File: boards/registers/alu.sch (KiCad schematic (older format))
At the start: 1 part, among them J1 ALU

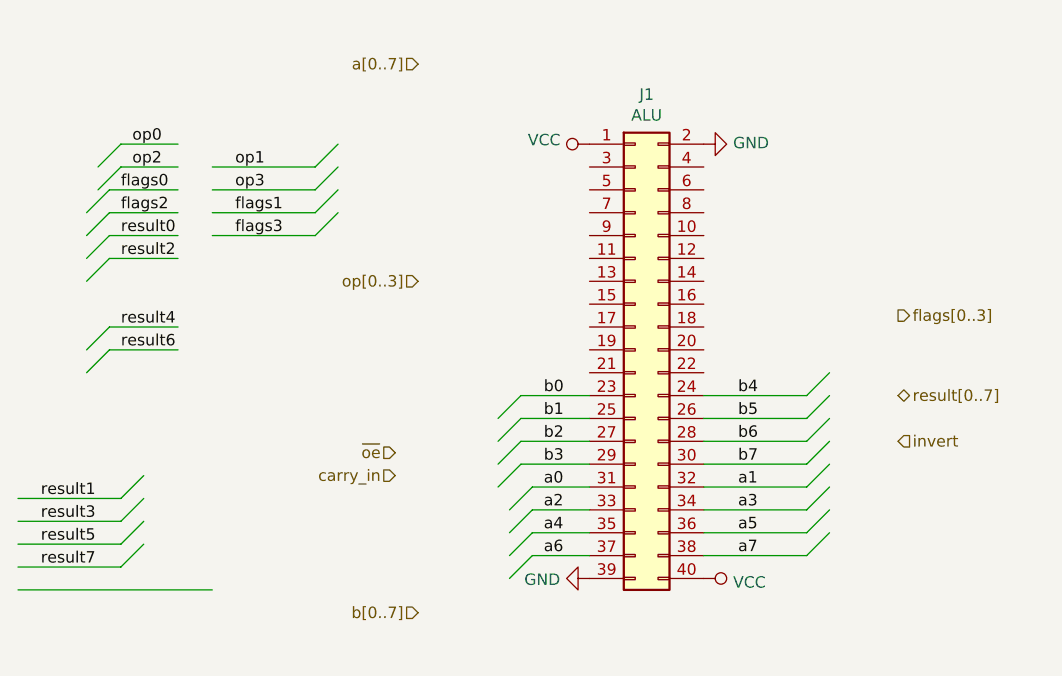
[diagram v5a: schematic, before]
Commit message: CPU registers board
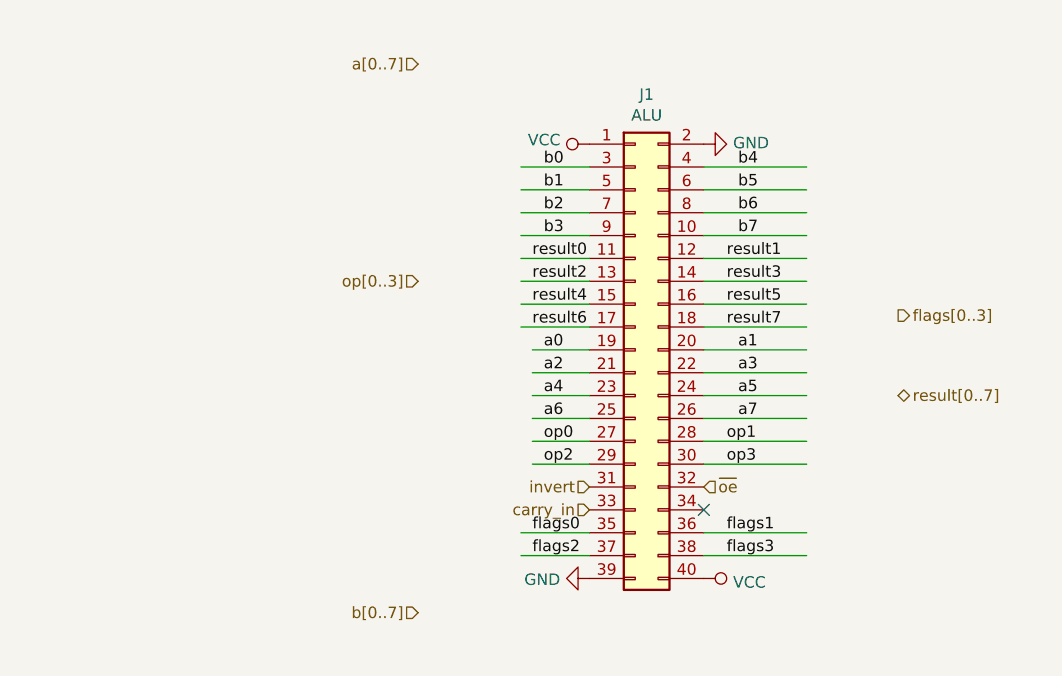
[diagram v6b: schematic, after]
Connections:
- wire segments 33 -> 32
- no-connect marks 0 -> 1
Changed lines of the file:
@@
 Text HLabel 3250 2400 0    50   Input ~ 0
 op[0..3]
-Text HLabel 3150 3150 0    50   Input ~ 0
+Text HLabel 4500 3300 2    50   Input ~ 0
 ~oe
-Text HLabel 3150 3250 0    50   Input ~ 0
+Text HLabel 4000 3400 0    50   Input ~ 0
 carry_in
-Text HLabel 5350 3100 2    50   Input ~ 0
+Text HLabel 4000 3300 0    50   Input ~ 0
 invert
 Text HLabel 5350 2900 2    50   3State ~ 0
@@
 	0    1    1    0
 $EndComp
-Entry Wire Line
-	3650 3400 3750 3300
-Entry Wire Line
-	3650 3500 3750 3400
-Entry Wire Line
-	3650 3600 3750 3500
-Entry Wire Line
-	3650 3700 3750 3600
-Entry Wire Line
-	3600 3000 3700 2900
-Entry Wire Line
-	3600 3100 3700 3000
-Entry Wire Line
-	3600 3200 3700 3100
-Entry Wire Line
-	3600 3300 3700 3200
 Wire Wire Line
-	3750 3300 4000 3300
+	3750 2700 4000 2700
 Wire Wire Line
-	4000 3400 3750 3400
+	4000 2800 3750 2800
 Wire Wire Line
-	3750 3500 4000 3500
+	3750 2900 4000 2900
 Wire Wire Line
-	4000 3600 3750 3600
-Entry Wire Line
-	4950 3300 5050 3200
-Entry Wire Line
-	4950 3400 5050 3300
-Entry Wire Line
-	4950 3500 5050 3400
-Entry Wire Line
-	4950 3600 5050 3500
-Entry Wire Line
-	4950 2900 5050 2800
-Entry Wire Line
-	4950 3000 5050 2900
-Entry Wire Line
-	4950 3100 5050 3000
-Entry Wire Line
-	4950 3200 5050 3100
-Text Label 3800 3300 0    50   ~ 0
+	4000 3000 3750 3000
+Text Label 3800 2700 0    50   ~ 0
 a0
-Text Label 3800 3400 0    50   ~ 0
+Text Label 3800 2800 0    50   ~ 0
 a2
-Text Label 3800 3500 0    50   ~ 0
+Text Label 3800 2900 0    50   ~ 0
 a4
-Text Label 3800 3600 0    50   ~ 0
+Text Label 3800 3000 0    50   ~ 0
 a6
-Text Label 4650 3300 0    50   ~ 0
+Text Label 4650 2700 0    50   ~ 0
 a1
-Text Label 4650 3400 0    50   ~ 0
+Text Label 4650 2800 0    50   ~ 0
 a3
-Text Label 4650 3500 0    50   ~ 0
+Text Label 4650 2900 0    50   ~ 0
 a5
-Text Label 4650 3600 0    50   ~ 0
+Text Label 4650 3000 0    50   ~ 0
 a7
+Wire Wire Line
+	4500 1900 4950 1900
+Wire Wire Line
+	4500 2000 4950 2000
+Wire Wire Line
+	4500 2100 4950 2100
+Wire Wire Line
+	4500 2200 4950 2200
+Wire Wire Line
+	3700 1900 4000 1900
+Wire Wire Line
+	4000 2000 3700 2000
+Wire Wire Line
+	3700 2100 4000 2100
+Wire Wire Line
+	4000 2200 3700 2200
+Text Label 3800 1900 0    50   ~ 0
+b0
+Text Label 3800 2100 0    50   ~ 0
+b2
+Text Label 4650 1900 0    50   ~ 0
+b4
+Text Label 4650 2100 0    50   ~ 0
+b6
+Text Label 3800 2000 0    50   ~ 0
+b1
+Text Label 3800 2200 0    50   ~ 0
+b3
+Text Label 4650 2000 0    50   ~ 0
+b5
+Text Label 4650 2200 0    50   ~ 0
+b7
+Wire Wire Line
+	4950 3100 4500 3100
+Wire Wire Line
+	4500 3200 4950 3200
+Text Label 4600 3100 0    50   ~ 0
+op1
+Text Label 4600 3200 0    50   ~ 0
+op3
+Wire Wire Line
+	3750 3100 4000 3100
+Wire Wire Line
+	4000 3200 3750 3200
+Text Label 3800 3100 0    50   ~ 0
+op0
+Text Label 3800 3200 0    50   ~ 0
+op2
+Wire Wire Line
+	4950 3500 4500 3500
+Wire Wire Line
+	4500 3600 4950 3600
+Text Label 3750 3500 0    50   ~ 0
+flags0
+Text Label 3750 3600 0    50   ~ 0
+flags2
+Text Label 4600 3500 0    50   ~ 0
+flags1
+Text Label 4600 3600 0    50   ~ 0
+flags3
+Wire Wire Line
+	4000 2600 3700 2600
+Wire Wire Line
+	3700 2500 4000 2500
+Wire Wire Line
+	4000 2400 3700 2400
+Wire Wire Line
+	3700 2300 4000 2300
+Text Label 3750 2300 0    50   ~ 0
+result0
+Text Label 3750 2400 0    50   ~ 0
+result2
+Text Label 3750 2500 0    50   ~ 0
+result4
+Text Label 3750 2600 0    50   ~ 0
+result6
+Wire Wire Line
+	3700 3600 4000 3600
+Wire Wire Line
+	4500 2700 4950 2700
+Wire Wire Line
+	4500 2800 4950 2800
 Wire Wire Line
 	4500 2900 4950 2900
@@
 	4500 3000 4950 3000
 Wire Wire Line
-	4500 3100 4950 3100
+	4950 2300 4500 2300
 Wire Wire Line
-	4500 3200 4950 3200
+	4500 2400 4950 2400
 Wire Wire Line
-	3700 2900 4000 2900
+	4950 2500 4500 2500
 Wire Wire Line
-	4000 3000 3700 3000
+	4500 2600 4950 2600
+Text Label 4600 2300 0    50   ~ 0
+result1
+Text Label 4600 2400 0    50   ~ 0
+result3
+Text Label 4600 2500 0    50   ~ 0
+result5
+Text Label 4600 2600 0    50   ~ 0
+result7
 Wire Wire Line
-	3700 3100 4000 3100
-Wire Wire Line
-	4000 3200 3700 3200
-Text Label 3800 2900 0    50   ~ 0
-b0
-Text Label 3800 3100 0    50   ~ 0
-b2
-Text Label 4650 2900 0    50   ~ 0
-b4
-Text Label 4650 3100 0    50   ~ 0
-b6
-Text Label 3800 3000 0    50   ~ 0
-b1
-Text Label 3800 3200 0    50   ~ 0
-b3
-Text Label 4650 3000 0    50   ~ 0
-b5
-Text Label 4650 3200 0    50   ~ 0
-b7
-Entry Wire Line
-	1850 1900 1950 1800
-Entry Wire Line
-	1850 2000 1950 1900
-Entry Wire Line
-	2800 1900 2900 1800
-Entry Wire Line
-	2800 2000 2900 1900
-Wire Wire Line
-	2800 1900 2350 1900
-Wire Wire Line
-	2350 2000 2800 2000
-Text Label 2450 1900 0    50   ~ 0
-op1
-Text Label 2450 2000 0    50   ~ 0
-op3
-Wire Wire Line
-	1950 1800 2200 1800
-Wire Wire Line
-	2200 1900 1950 1900
-Text Label 2000 1800 0    50   ~ 0
-op0
-Text Label 2000 1900 0    50   ~ 0
-op2
-Entry Wire Line
-	1800 2100 1900 2000
-Entry Wire Line
-	1800 2200 1900 2100
-Entry Wire Line
-	2800 2100 2900 2000
-Entry Wire Line
-	2800 2200 2900 2100
-Wire Wire Line
-	2800 2100 2350 2100
-Wire Wire Line
-	2350 2200 2800 2200
-Text Label 1950 2000 0    50   ~ 0
-flags0
-Text Label 1950 2100 0    50   ~ 0
-flags2
-Text Label 2450 2100 0    50   ~ 0
-flags1
-Text Label 2450 2200 0    50   ~ 0
-flags3
-Text Label 1600 3650 0    50   ~ 0
-result7
-Text Label 1600 3550 0    50   ~ 0
-result5
-Text Label 1600 3450 0    50   ~ 0
-result3
-Text Label 1600 3350 0    50   ~ 0
-result1
-Wire Wire Line
-	1500 3650 1950 3650
-Wire Wire Line
-	1950 3550 1500 3550
-Wire Wire Line
-	1500 3450 1950 3450
-Wire Wire Line
-	1950 3350 1500 3350
-Entry Wire Line
-	1950 3350 2050 3250
-Entry Wire Line
-	1950 3450 2050 3350
-Entry Wire Line
-	1950 3550 2050 3450
-Entry Wire Line
-	1950 3650 2050 3550
-Entry Wire Line
-	1800 2800 1900 2700
-Entry Wire Line
-	1800 2700 1900 2600
-Entry Wire Line
-	1800 2400 1900 2300
-Entry Wire Line
-	1800 2300 1900 2200
-Wire Wire Line
-	2200 2700 1900 2700
-Wire Wire Line
-	1900 2600 2200 2600
-Wire Wire Line
-	2200 2300 1900 2300
-Wire Wire Line
-	1900 2200 2200 2200
-Text Label 1950 2200 0    50   ~ 0
-result0
-Text Label 1950 2300 0    50   ~ 0
-result2
-Text Label 1950 2600 0    50   ~ 0
-result4
-Text Label 1950 2700 0    50   ~ 0
-result6
-Wire Wire Line
-	1900 2000 2200 2000
-Wire Wire Line
-	1900 2100 2200 2100
-Wire Wire Line
-	2350 3750 1500 3750
-Wire Wire Line
-	4500 3300 4950 3300
-Wire Wire Line
-	4500 3400 4950 3400
-Wire Wire Line
-	4500 3500 4950 3500
-Wire Wire Line
-	4500 3600 4950 3600
+	4000 3500 3700 3500
+NoConn ~ 4500 3400
 $EndSCHEMATC

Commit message: Part names
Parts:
- J1: value ALU -> SSW-120-02-G-D-RA
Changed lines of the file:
@@
 P 4200 2700
 F 0 "J1" H 4250 3817 50  0000 C CNN
-F 1 "ALU" H 4250 3726 50  0000 C CNN
+F 1 "SSW-120-02-G-D-RA" H 4250 3726 50  0000 C CNN
 F 2 "Connector_PinSocket_2.54mm:PinSocket_2x20_P2.54mm_Horizontal" H 4200 2700 50  0001 C CNN
 F 3 "~" H 4200 2700 50  0001 C CNN
